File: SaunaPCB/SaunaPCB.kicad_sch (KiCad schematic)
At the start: 0 parts

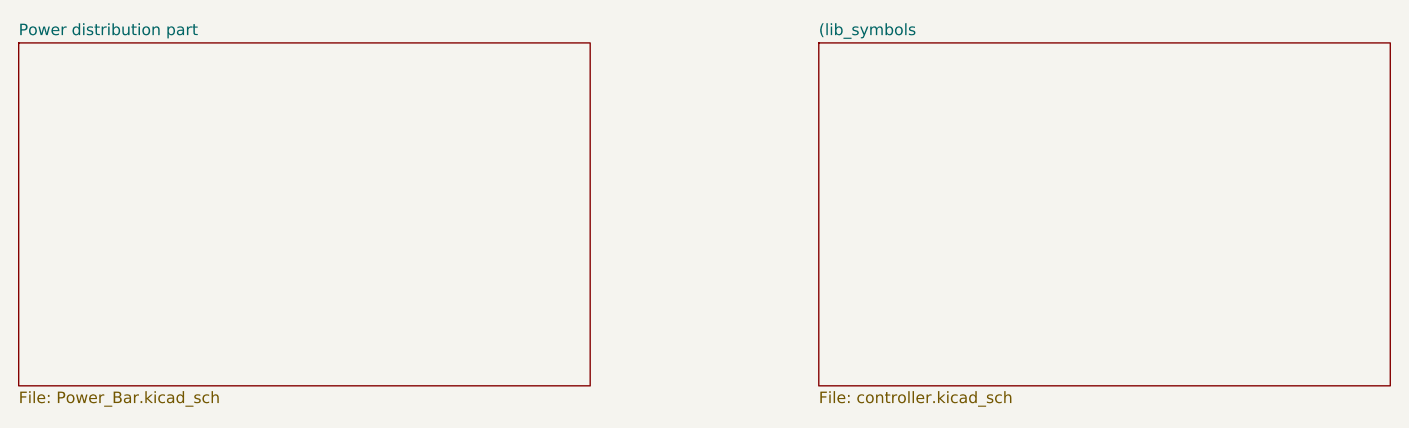
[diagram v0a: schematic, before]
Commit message: Working on schematic and PCB -AC/DC and DC/DC converters with correct symbol and footprint now - rough placement of the power parts
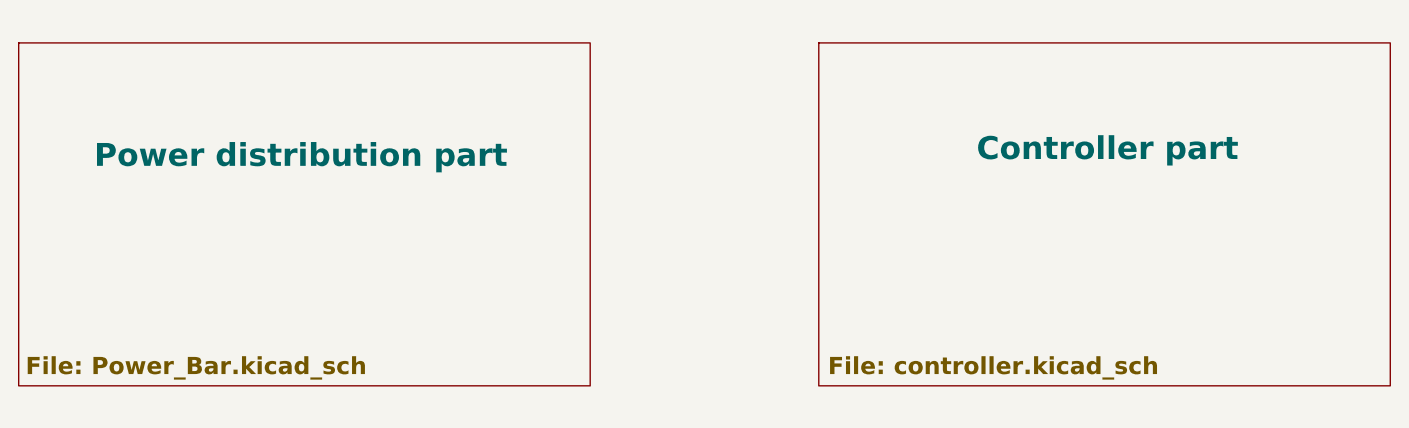
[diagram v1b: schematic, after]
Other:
- sheet (lib_symbols renamed Controller part
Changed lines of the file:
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@@
 		(on_board yes)
 		(dnp no)
-		(fields_autoplaced yes)
 		(stroke
 			(width 0.1524)
@@
 		)
 		(fill
-			(color 0 0 0 0.0000)
+			(color 222 221 53 1.0000)
 		)
 		(property "Sheetname" "Power distribution part"
-			(at 25.4 24.6884 0)
+			(at 33.782 39.37 0)
 			(effects
 				(font
-					(size 1.27 1.27)
+					(size 2.54 2.54)
+					(thickness 0.508)
+					(bold yes)
 				)
 				(justify left bottom)
@@
 		)
 		(property "Sheetfile" "Power_Bar.kicad_sch"
-			(at 25.4 64.0846 0)
+			(at 26.162 60.198 0)
 			(effects
 				(font
-					(size 1.27 1.27)
+					(size 1.905 1.905)
+					(thickness 0.381)
+					(bold yes)
 				)
 				(justify left top)
@@
 		(on_board yes)
 		(dnp no)
-		(fields_autoplaced yes)
 		(stroke
 			(width 0.1524)
@@
 		)
 		(fill
-			(color 0 0 0 0.0000)
+			(color 222 221 53 1.0000)
 		)
+		(property "Sheetname" "Controller part"
+			(at 131.826 38.608 0)
+			(effects
+				(font
+					(size 2.54 2.54)
+					(thickness 0.508)
+					(bold yes)
+				)
+				(justify left bottom)
+			)
+		)
+		(property "Sheetfile" "controller.kicad_sch"
+			(at 115.316 60.198 0)
+			(effects
+				(font
+					(size 1.905 1.905)
+					(thickness 0.381)
+					(bold yes)
+				)
+				(justify left top)
+			)
+		)
+		(instances
+			(project "SaunaPCB"
+				(path "/e6d8484d-2bb5-441d-9b2b-e37a9f2fa458"
+					(page "3")
+				)
+			)
+		)
+	)
 	(sheet_instances
 		(path "/"
